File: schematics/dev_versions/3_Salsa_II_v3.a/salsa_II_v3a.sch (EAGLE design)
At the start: 53 parts, among them IC1 L293DD, IC2 74HCT04D, Q2 PMV20EN, Q3 PMV20EN, Q4 PMV20EN, Q5 PMV20EN, U1 ATMEGA168

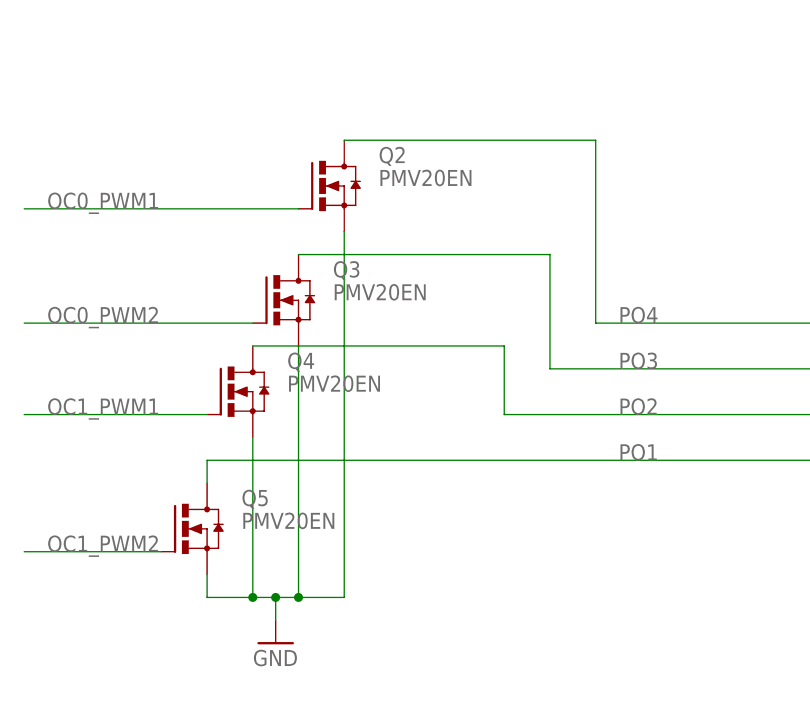
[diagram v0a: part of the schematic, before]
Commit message: moved version 3 to dev as 3b was ordered
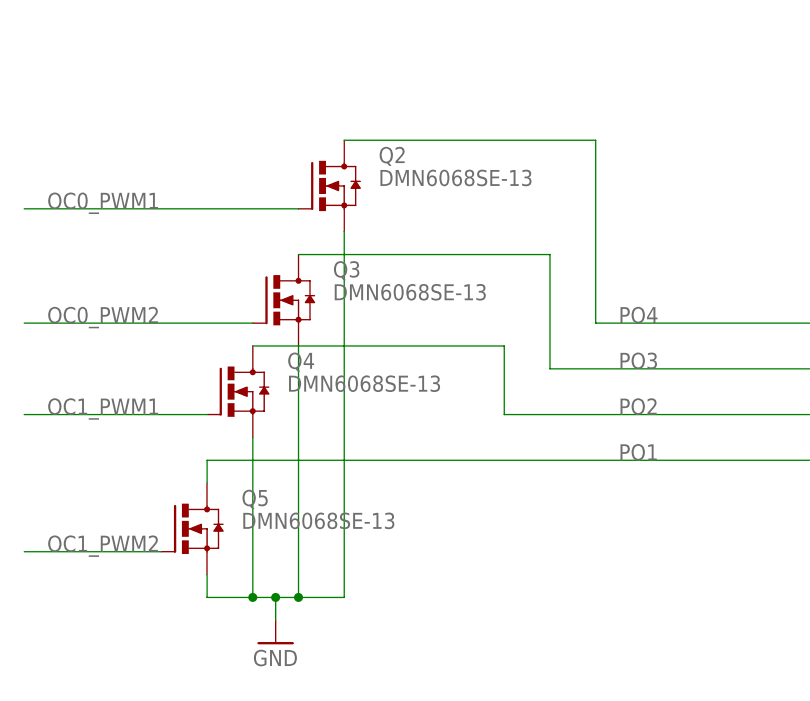
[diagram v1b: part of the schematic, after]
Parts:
- Q2, Q3, Q4, Q5: value PMV20EN -> DMN6068SE-13
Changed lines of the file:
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@@
 <part name="U1" library="SparkFun-DigitalIC" deviceset="ATMEGA168" device=""/>
 <part name="JP2" library="pinhead" deviceset="PINHD-2X3" device=""/>
-<part name="Q2" library="transistor-power" deviceset="NMOSFET_SMD_223" device="" value="PMV20EN"/>
-<part name="Q3" library="transistor-power" deviceset="NMOSFET_SMD_223" device="" value="PMV20EN"/>
-<part name="Q4" library="transistor-power" deviceset="NMOSFET_SMD_223" device="" value="PMV20EN"/>
-<part name="Q5" library="transistor-power" deviceset="NMOSFET_SMD_223" device="" value="PMV20EN"/>
+<part name="Q2" library="transistor-power" deviceset="NMOSFET_SMD_223" device="" value="DMN6068SE-13"/>
+<part name="Q3" library="transistor-power" deviceset="NMOSFET_SMD_223" device="" value="DMN6068SE-13"/>
+<part name="Q4" library="transistor-power" deviceset="NMOSFET_SMD_223" device="" value="DMN6068SE-13"/>
+<part name="Q5" library="transistor-power" deviceset="NMOSFET_SMD_223" device="" value="DMN6068SE-13"/>
 <part name="PAD_G1" library="wirepad" deviceset="3,17/1,3" device=""/>
 <part name="PAD_VIN" library="wirepad" deviceset="3,17/1,3" device=""/>
